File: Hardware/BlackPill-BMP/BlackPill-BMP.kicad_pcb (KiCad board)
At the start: 2 copper layers, 72.4 x 60 mm, 40 parts, among them J1 JTAG, J2 VCC, J3 GND, J4 SWO, J5 GDB_COMM, J6 TVCC, J7 LogicAna, J8 Conn_01x10, J9 Conn_01x11, U1 BlueAndBlackPill, U2 AD8531ARTZ, U3 SRV05-4, U4 TXS0108EPW, U5 SRV05-4

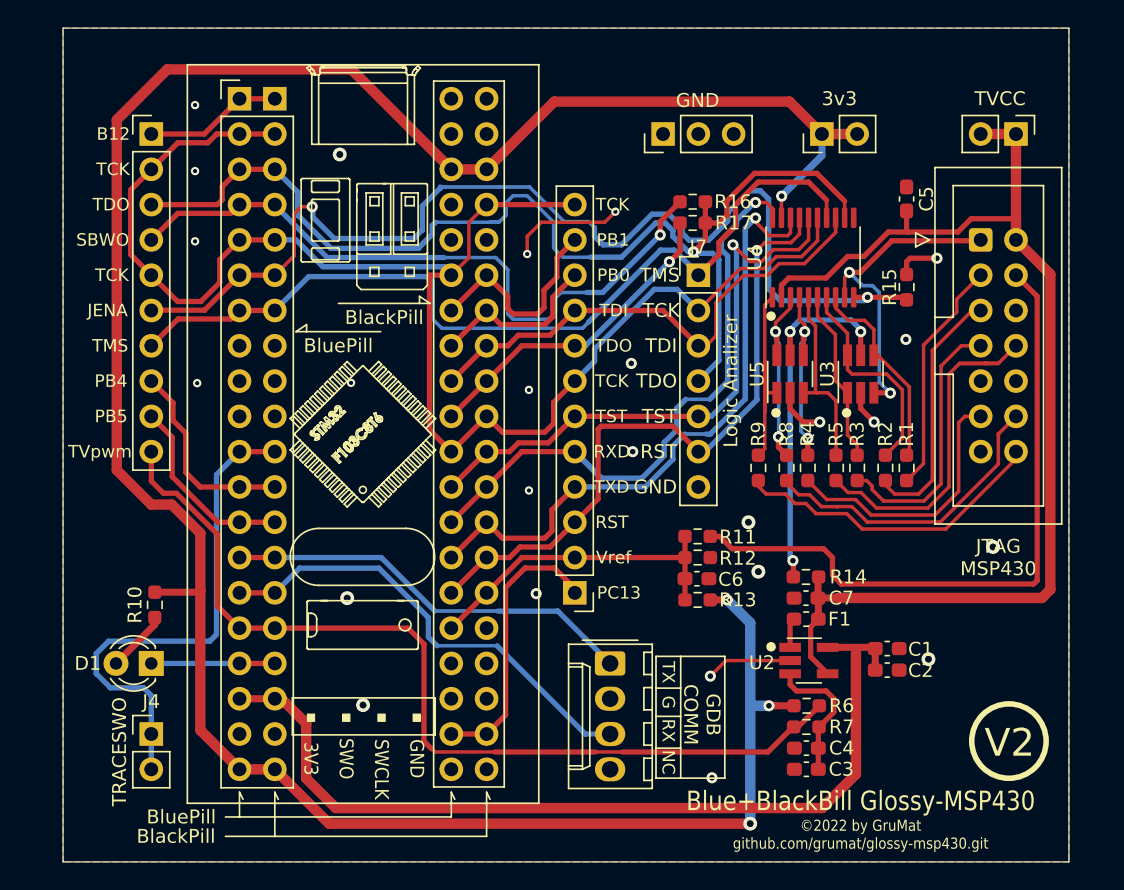
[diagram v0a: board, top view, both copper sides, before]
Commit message: Changed TXS0108 for TXB0304. for lower impedance. Using ESD protection of those parts.
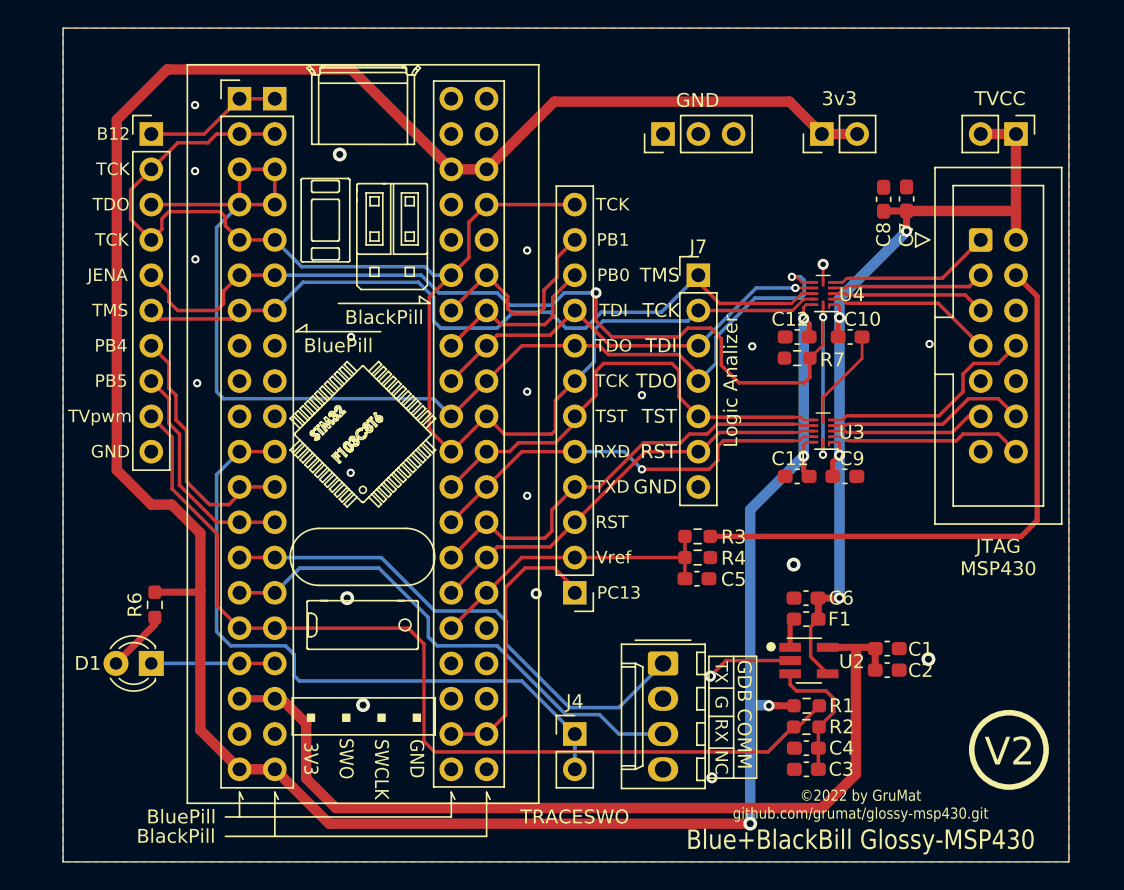
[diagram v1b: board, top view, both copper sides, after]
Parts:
- removed the R1 at (177.5, 96.6)
- removed R13: 470K, Resistor_SMD:R_0603_1608Metric_Pad0.98x0.95mm_HandSolder
- removed R14: 10K, Resistor_SMD:R_0603_1608Metric_Pad0.98x0.95mm_HandSolder
- removed R16, R8, R9: 330, Resistor_SMD:R_0603_1608Metric_Pad0.98x0.95mm_HandSolder
- removed R17: 22, Resistor_SMD:R_0603_1608Metric_Pad0.98x0.95mm_HandSolder
- removed the R2 at (176.0, 96.6)
- removed the R3 at (174.0, 96.6)
- removed the R4 at (170.4, 96.6)
- removed R5: 100, Resistor_SMD:R_0603_1608Metric_Pad0.98x0.95mm_HandSolder
- removed the U3 at (174.2, 89.9)
- removed U5: SRV05-4, Package_TO_SOT_SMD:SOT-23-6_Handsoldering
- added C10: 100nF, Capacitor_SMD:C_0603_1608Metric_Pad1.08x0.95mm_HandSolder, F.Cu at (173.5, 87.2)
- added C11: 100nF, Capacitor_SMD:C_0603_1608Metric_Pad1.08x0.95mm_HandSolder, F.Cu at (169.7, 97.3)
- added C12: 100nF, Capacitor_SMD:C_0603_1608Metric_Pad1.08x0.95mm_HandSolder, F.Cu at (169.7, 87.2)
- added C8: 10uF, Capacitor_SMD:C_0603_1608Metric_Pad1.08x0.95mm_HandSolder, F.Cu at (175.9, 77.3)
- added C9: 100nF, Capacitor_SMD:C_0603_1608Metric_Pad1.08x0.95mm_HandSolder, F.Cu at (173.1, 97.3)
- added U4: TXBN0304RUT, Package_DFN_QFN:Texas_R_PUQFN-N12, F.Cu at (171.5, 84.1)
- U3: renamed from U4; value TXS0108EPW -> TXB0108EPW; footprint Package_SO:TSSOP-20_4.4x6.5mm_P0.65mm -> Package_DFN_QFN:Texas_R_PUQFN-N12
- moved J4 30.5 mm to (153.7, 115.8)
- moved U3 12.5 mm to (171.5, 94.0), turned to 180 degrees
- moved R7 9.39 mm to (169.7, 88.7), turned to 0 degrees
- moved J5 3.81 mm to (160.0, 110.7)
- renumbered C6 to C5, C7 to C6, C5 to C7, R6 to R1, R7 to R2, R11 to R3, R12 to R4, R10 to R6, R15 to R7
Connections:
- J7 pad 4: /LTDO -> /mTDO
- J8 pad 10: /TV_PWM -> GND
- J8 pad 3: /LTDO -> /mTDO
- J8 pad 4: /SBWO -> /mTCK
- J8 pad 5: /mTCK -> /JENA
- J8 pad 6: /JENA -> /mTMS
- J8 pad 7: /mTMS -> /PB4
- J8 pad 8: /PB4 -> /PB5
- J8 pad 9: /PB5 -> /TV_PWM
- U1 pad A3: /LTDO -> /mTDO
- U1 pad A4: /SBWO -> /mTDO
- U1 pad B3: /LTDO -> /mTDO
- U1 pad B4: /SBWO -> /mTDO
- U3 pad 1: /LRXD -> /TVCC
- U3 pad 10: /JENA -> /mRXD
- U3 pad 11: GND -> +3V3
- U3 pad 12: /LTDO -> /JENA
- U3 pad 2: /TVCC -> /JRXD
- U3 pad 3: /LTXD -> /JRST
- U3 pad 4: /LRST -> /JTXD
- U3 pad 5: /LTEST -> /JTEST
- U3 pad 6: /LTCK -> GND
- U3 pad 7: /LTMS -> /mTEST
- U3 pad 8: /LTDI -> /mTXD
- U3 pad 9: /JTDO -> /mRST
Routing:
- net /LTDO: track 81.5 -> 0.00 mm, vias 1 -> 0
- net /mTDO: track 23.4 -> 84.6 mm
- net /SBWO: track 49.1 -> 0.00 mm, vias 1 -> 0
- net Net-(R14-Pad2): track 27.1 -> 0.00 mm, vias 3 -> 0
- net +3V3: track 182.2 -> 201.2 mm
- net /TVCC: track 82.3 -> 63.3 mm, vias 0 -> 4
- net /mRST: track 47.7 -> 30.9 mm, vias 1 -> 0
- net /LRXD: track 16.3 -> 0.00 mm
- net /mRXD: track 46.2 -> 30.3 mm
- net /LTMS: track 15.6 -> 0.00 mm
- net /mTMS: track 70.2 -> 55.4 mm
- net /LTDI: track 14.5 -> 0.00 mm
- net /mTXD: track 46.0 -> 32.0 mm, vias 1 -> 0
- net /LTXD: track 13.9 -> 0.00 mm, vias 2 -> 0
- net /LTEST: track 13.6 -> 0.00 mm
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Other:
- board text removed: "SBWO"

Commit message: Updated Blue-Black-Pill prototype board.
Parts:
- added C9: 100nF, Capacitor_SMD:C_0603_1608Metric_Pad1.08x0.95mm_HandSolder, F.Cu at (123.1, 88.0)
- added D1: 82356050050, Diode_SMD:D_0603_1608Metric_Pad1.05x0.95mm_HandSolder, F.Cu at (162.5, 103.1)
- added J9: Conn_01x05_Male, Connector_PinHeader_2.54mm:PinHeader_1x05_P2.54mm_Vertical, F.Cu at (123.2, 95.5)
- added U3: SN74LVC1G125, Package_TO_SOT_SMD:SOT-23-5, F.Cu at (122.9, 90.7)
- J10: renamed from J9; value Conn_01x11 -> Conn_01x12_Male
- J8: value Conn_01x10 -> Conn_01x06_Male; footprint Connector_PinHeader_2.54mm:PinHeader_1x10_P2.54mm_Vertical -> Connector_PinHeader_2.54mm:PinHeader_1x06_P2.54mm_Vertical
- moved J10 27.9 mm to (153.7, 77.7), turned to 0 degrees
- moved C8 9.40 mm to (184.8, 80.4), turned to 90 degrees
- moved J1 7.62 mm to (182.9, 87.9)
- moved R5 7.30 mm to (122.7, 113.8), turned to 0 degrees
- moved C7 6.50 mm to (183.2, 80.4), turned to 90 degrees
- moved R4 3.05 mm to (162.5, 106.1)
- renumbered C9 to C10, C10 to C11, C11 to C12, C12 to C13, D1 to D2, R6 to R5, R7 to R6, U3 to U4, U4 to U5
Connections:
- C10 pad 2: /TVCC -> VCC
- C11 pad 2: /TVCC -> VCC
- C6 pad 2: /TVCC -> VCC
- C7 pad 2: /TVCC -> VCC
- C8 pad 2: /TVCC -> VCC
- D2 pad 1: /LEDG -> GND
- F1 pad 2: /TVCC -> VCC
- J1 pad 2: /TVCC -> VCC
- J10 pad 1: /PC13 -> /mTCK
- J10 pad 10: /PB0 -> /mRST
- J10 pad 11: /PB1 -> /VREF_2
- J10 pad 12: /mTCK -> /LEDS
- J10 pad 2: /VREF_2 -> /PB1
- J10 pad 3: /mRST -> /PB0
- J10 pad 4: /mTXD -> /mTDI
- J10 pad 5: /mRXD -> /mTDO
- J10 pad 6: /mTEST -> /mTCK
- J10 pad 7: /mTCK -> /mTEST
- J10 pad 8: /mTDO -> /mRXD
- J10 pad 9: /mTDI -> /mTXD
- J5 pad 4: unconnected-(J5-Pad4) -> VCC
- J6 pad 1: /TVCC -> VCC
- J6 pad 2: /TVCC -> VCC
- J8 pad 1: /PB12 -> /JENA
- J8 pad 4: /mTCK -> /SBWO
- J8 pad 5: /JENA -> /mTCK
- J8 pad 6: /mTMS -> /SBW_DIR
- R5 pad 2: +3V3 -> /LEDS
- U1 pad A1: /PB12 -> /JENA
- U1 pad A17: /LEDG -> /PB9
- U1 pad A22: /PC13 -> /LEDS
- U1 pad A4: /mTDO -> /SBWO
- U1 pad A6: /JENA -> /SBW_DIR
- U1 pad B1: /PB12 -> /JENA
- U1 pad B17: /LEDG -> /PB9
- U1 pad B22: /PC13 -> /LEDS
- U1 pad B4: /mTDO -> /SBWO
- U1 pad B6: /JENA -> /SBW_DIR
- U2 pad 4: /TVCC -> VCC
- U4 pad 1: /TVCC -> VCC
- U5 pad 1: /TVCC -> VCC
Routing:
- net VCC: track 0.00 -> 96.8 mm, vias 0 -> 4
- net /TVCC: track 63.3 -> 0.00 mm, vias 4 -> 0
- net /LEDS: track 0.00 -> 50.2 mm
- net /SBW_DIR: track 0.00 -> 24.0 mm
- net /SBWO: track 0.00 -> 22.7 mm
- net /PC13: track 20.1 -> 0.00 mm
- net /PB9: track 0.00 -> 18.1 mm
- net /mTMS: track 55.4 -> 72.8 mm
- net +3V3: track 201.2 -> 212.6 mm, vias 4 -> 6
- net /JENA: track 73.8 -> 84.3 mm
- net /PB12: track 9.94 -> 0.00 mm
- net /LEDG: track 8.89 -> 0.00 mm
- net /JTCK: track 12.1 -> 19.8 mm
- net /TV_PWM: track 69.1 -> 62.4 mm
- net /JTMS: track 11.2 -> 17.9 mm
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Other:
- board text added: "LEDS"
- board text added: "PB9"
- board text added: "SBWD"
- board text added: "SBWO"
- board text added: "VC"
- board text removed: "B12"
- board text removed: "NC"
- board text removed: "PC13"

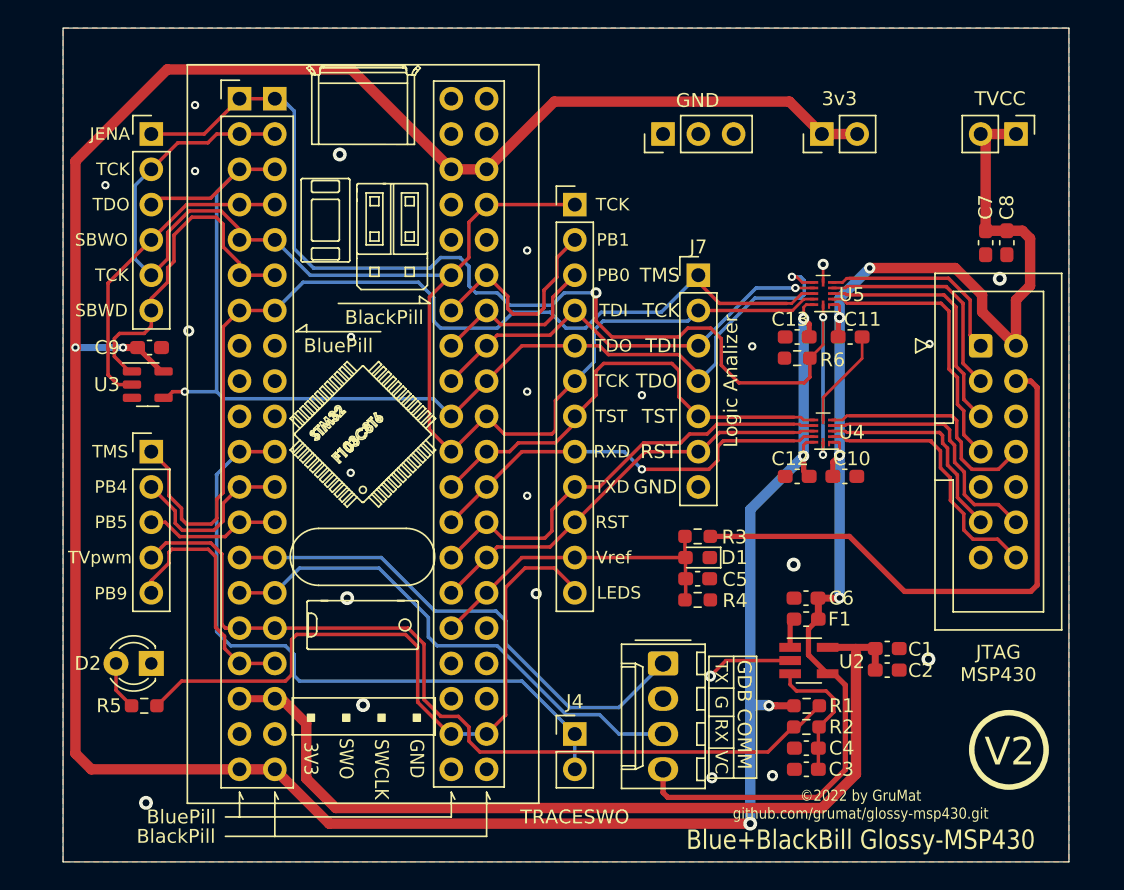
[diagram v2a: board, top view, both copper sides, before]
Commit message: Complete review of output stage of Proto board
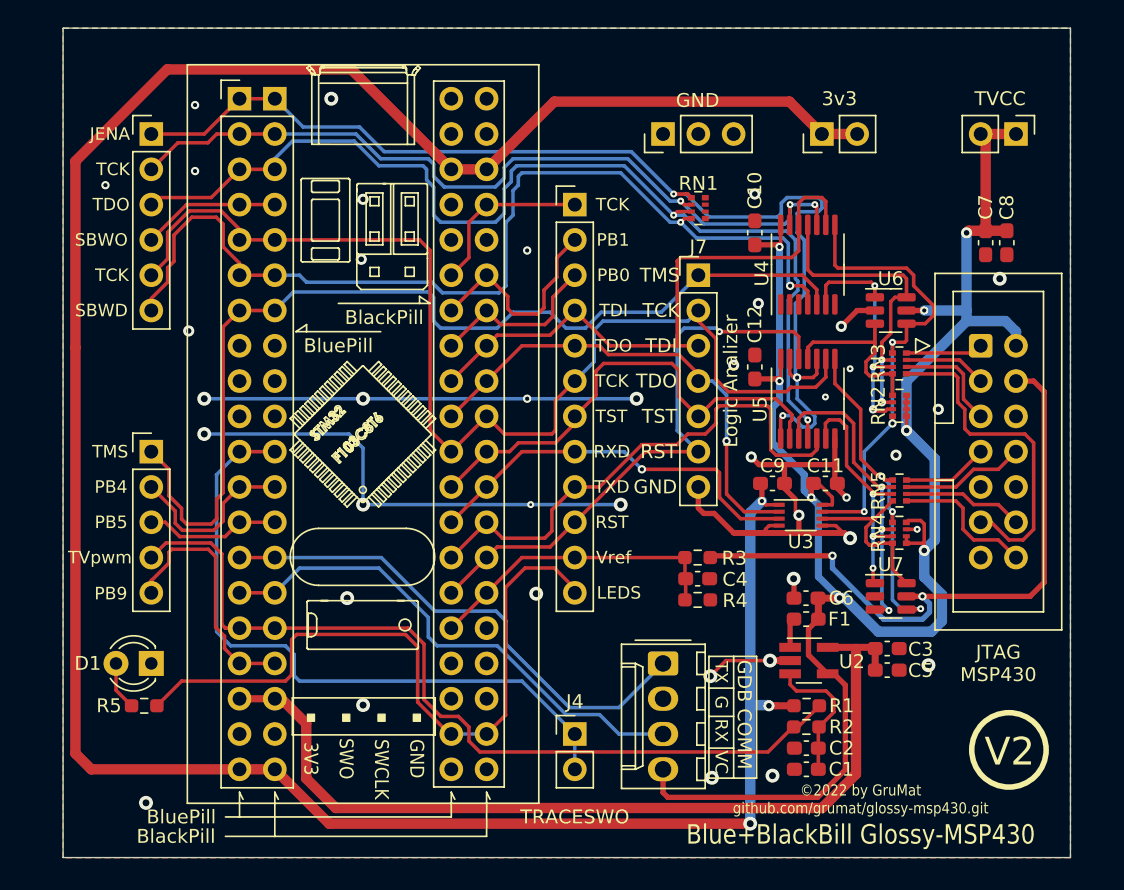
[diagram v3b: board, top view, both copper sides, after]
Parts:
- removed C13: 100nF, Capacitor_SMD:C_0603_1608Metric_Pad1.08x0.95mm_HandSolder
- removed the D1 at (162.5, 103.1)
- removed R6: 47K, Resistor_SMD:R_0603_1608Metric_Pad0.98x0.95mm_HandSolder
- added RN1: 47k, Resistor_SMD:R_Array_Convex_4x0402, F.Cu at (162.6, 78.0)
- added RN2: 47k, Resistor_SMD:R_Array_Convex_4x0402, F.Cu at (177.0, 92.2)
- added RN3: 47, Resistor_SMD:R_Array_Convex_4x0402, F.Cu at (177.0, 89.1)
- added RN4: 47k, Resistor_SMD:R_Array_Convex_4x0402, F.Cu at (177.0, 101.3)
- added RN5: 47, Resistor_SMD:R_Array_Convex_4x0402, F.Cu at (177.0, 98.3)
- added U6: SRV05-4, Package_TO_SOT_SMD:SOT-23-6, F.Cu at (176.4, 85.3)
- added U7: SRV05-4, Package_TO_SOT_SMD:SOT-23-6, F.Cu at (176.4, 105.9)
- U3: value SN74LVC1G125 -> 74LVC2T45DC; footprint Package_TO_SOT_SMD:SOT-23-5 -> Package_SO:VSSOP-8_2.3x2mm_P0.5mm
- U4: value TXB0108EPW -> 74LS126; footprint Package_DFN_QFN:Texas_R_PUQFN-N12 -> Package_SO:TSSOP-14_4.4x5mm_P0.65mm
- U5: value TXBN0304RUT -> 74LS126; footprint Package_DFN_QFN:Texas_R_PUQFN-N12 -> Package_SO:TSSOP-14_4.4x5mm_P0.65mm
- moved U3 47.9 mm to (169.9, 100.1)
- moved C12 43.6 mm to (166.6, 89.4), turned to -90 degrees
- moved U4 12.0 mm to (170.4, 82.0), turned to 90 degrees
- moved C10 10.2 mm to (166.6, 79.7), turned to -90 degrees
- moved U5 7.65 mm to (170.4, 91.7), turned to 90 degrees
- moved C9 1.85 mm to (167.9, 97.8), turned to 180 degrees
- moved R3 1.52 mm to (162.5, 103.1)
- moved C11 1.49 mm to (171.7, 97.8)
- renumbered C3 to C1, C11 to C10, C10 to C11, C9 to C12, C4 to C2, C1 to C3, C5 to C4, C2 to C5, C12 to C9, D2 to D1
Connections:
- C12 pad 2: +3V3 -> VCC
- J10 pad 1: /mTCK -> /PB10
- J8 pad 1: /JENA -> /ENA1
- J8 pad 2: /mTCK -> /ENA2
- J8 pad 3: /mTDO -> /ENA3
- J8 pad 4: /SBWO -> /PB15
- J8 pad 6: /SBW_DIR -> /SBWO
- U1 pad A1: /JENA -> /ENA1
- U1 pad A2: /mTCK -> /ENA2
- U1 pad A3: /mTDO -> /ENA3
- U1 pad A35: /mTCK -> /PB10
- U1 pad A4: /SBWO -> /PB15
- U1 pad A6: /SBW_DIR -> /SBWO
- U1 pad B1: /JENA -> /ENA1
- U1 pad B2: /mTCK -> /ENA2
- U1 pad B3: /mTDO -> /ENA3
- U1 pad B37: /mTCK -> /PB10
- U1 pad B4: /SBWO -> /PB15
- U1 pad B6: /SBW_DIR -> /SBWO
- U3 pad 1: /SBW_DIR -> +3V3
- U3 pad 2: /SBWO -> /mTDO
- U3 pad 3: GND -> /mRXD
- U3 pad 4: /mTDO -> GND
- U3 pad 5: +3V3 -> GND
- U4 pad 1: VCC -> GND
- U4 pad 10: /mRXD -> /ENA2
- U4 pad 11: +3V3 -> /rTDI
- U4 pad 12: /JENA -> /mTDI
- U4 pad 2: /JRXD -> GND
- U4 pad 3: /JRST -> unconnected-(U4-Pad3)
- U4 pad 4: /JTXD -> /SBWO
- U4 pad 5: /JTEST -> /mTMS
- U4 pad 6: GND -> /rTMS
- U4 pad 7: /mTEST -> GND
- U4 pad 8: /mTXD -> /rTDO
- U4 pad 9: /mRST -> /mTDI
- U5 pad 1: VCC -> /ENA1
- U5 pad 10: /mTCK -> /ENA1
- U5 pad 11: +3V3 -> /rRST
- U5 pad 12: /JENA -> /mRST
- U5 pad 2: /JTCK -> /mTEST
- U5 pad 3: /JTMS -> /rTEST
- U5 pad 4: /JTDI -> /ENA3
- U5 pad 5: /JTDO -> /mTXD
- U5 pad 6: GND -> /rTXD
- U5 pad 7: /mTDO -> GND
- U5 pad 8: /mTDI -> /rTCK
- U5 pad 9: /mTMS -> /mTCK
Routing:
- net GND: track 14.6 -> 117.3 mm, vias 24 -> 40
- net /JENA: track 84.3 -> 0.00 mm, vias 3 -> 0
- net /ENA1: track 0.00 -> 82.7 mm, vias 0 -> 3
- net /ENA3: track 0.00 -> 74.7 mm, vias 0 -> 2
- net /ENA2: track 0.00 -> 59.2 mm, vias 0 -> 3
- net /mTDO: track 84.4 -> 35.1 mm, vias 2 -> 1
- net /SBWO: track 22.7 -> 70.7 mm, vias 0 -> 2
- net VCC: track 96.8 -> 140.2 mm, vias 4 -> 8
- net /rTDO: track 0.00 -> 34.2 mm, vias 0 -> 3
- net /mTCK: track 106.3 -> 81.0 mm
- net +3V3: track 212.6 -> 187.6 mm, vias 6 -> 3
- net /rTCK: track 0.00 -> 24.2 mm, vias 0 -> 3
- net /SBW_DIR: track 24.0 -> 0.00 mm
- net /rTEST: track 0.00 -> 23.1 mm, vias 0 -> 3
- net /rTDI: track 0.00 -> 22.3 mm, vias 0 -> 2
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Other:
- board size 72.4 x 60 mm -> 72.5 x 59.7 mm

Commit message: Fixed an error on the TDI/TDO line selection
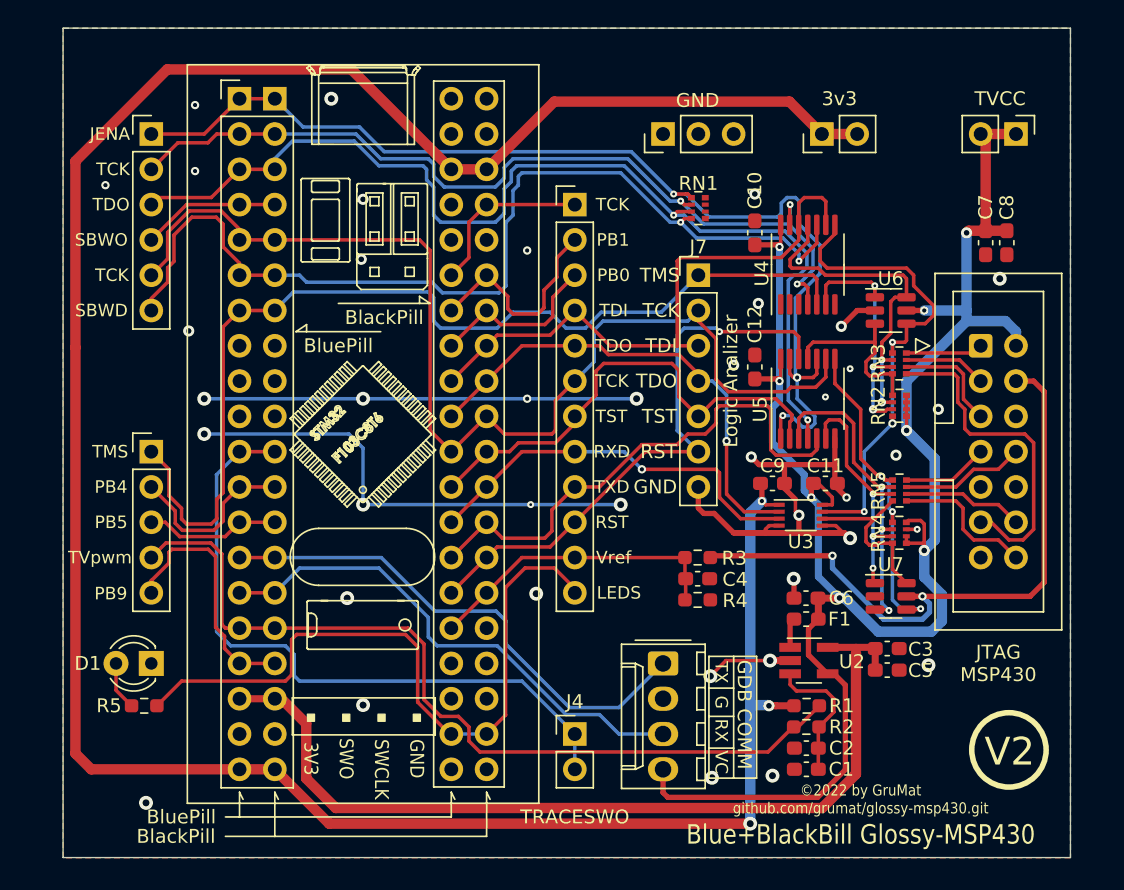
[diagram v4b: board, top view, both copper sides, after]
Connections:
- U4 pad 10: /ENA2 -> /SBWO
- U4 pad 4: /SBWO -> /ENA2
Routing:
- net /ENA2: track 59.2 -> 63.7 mm
- net /ENA1: track 82.7 -> 80.4 mm
- net /rTDI: track 22.3 -> 23.9 mm
- net /rTDO: track 34.2 -> 35.5 mm
- net /SBWO: track 70.7 -> 69.9 mm
- net /ENA3: track 74.7 -> 75.4 mm

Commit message: - Components review
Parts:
- RN3, RN5: value 47 -> 100
